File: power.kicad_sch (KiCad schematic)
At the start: 83 parts, among them Q1 BSS138AKA, Q2 SQS401EN-T1_BE3, Q3 BCM857BS-7-F, U3 LMR62014XMF, U4 AP62301_TSOT, U5 AP62301_TSOT, U6 AP22615A_TSOT26

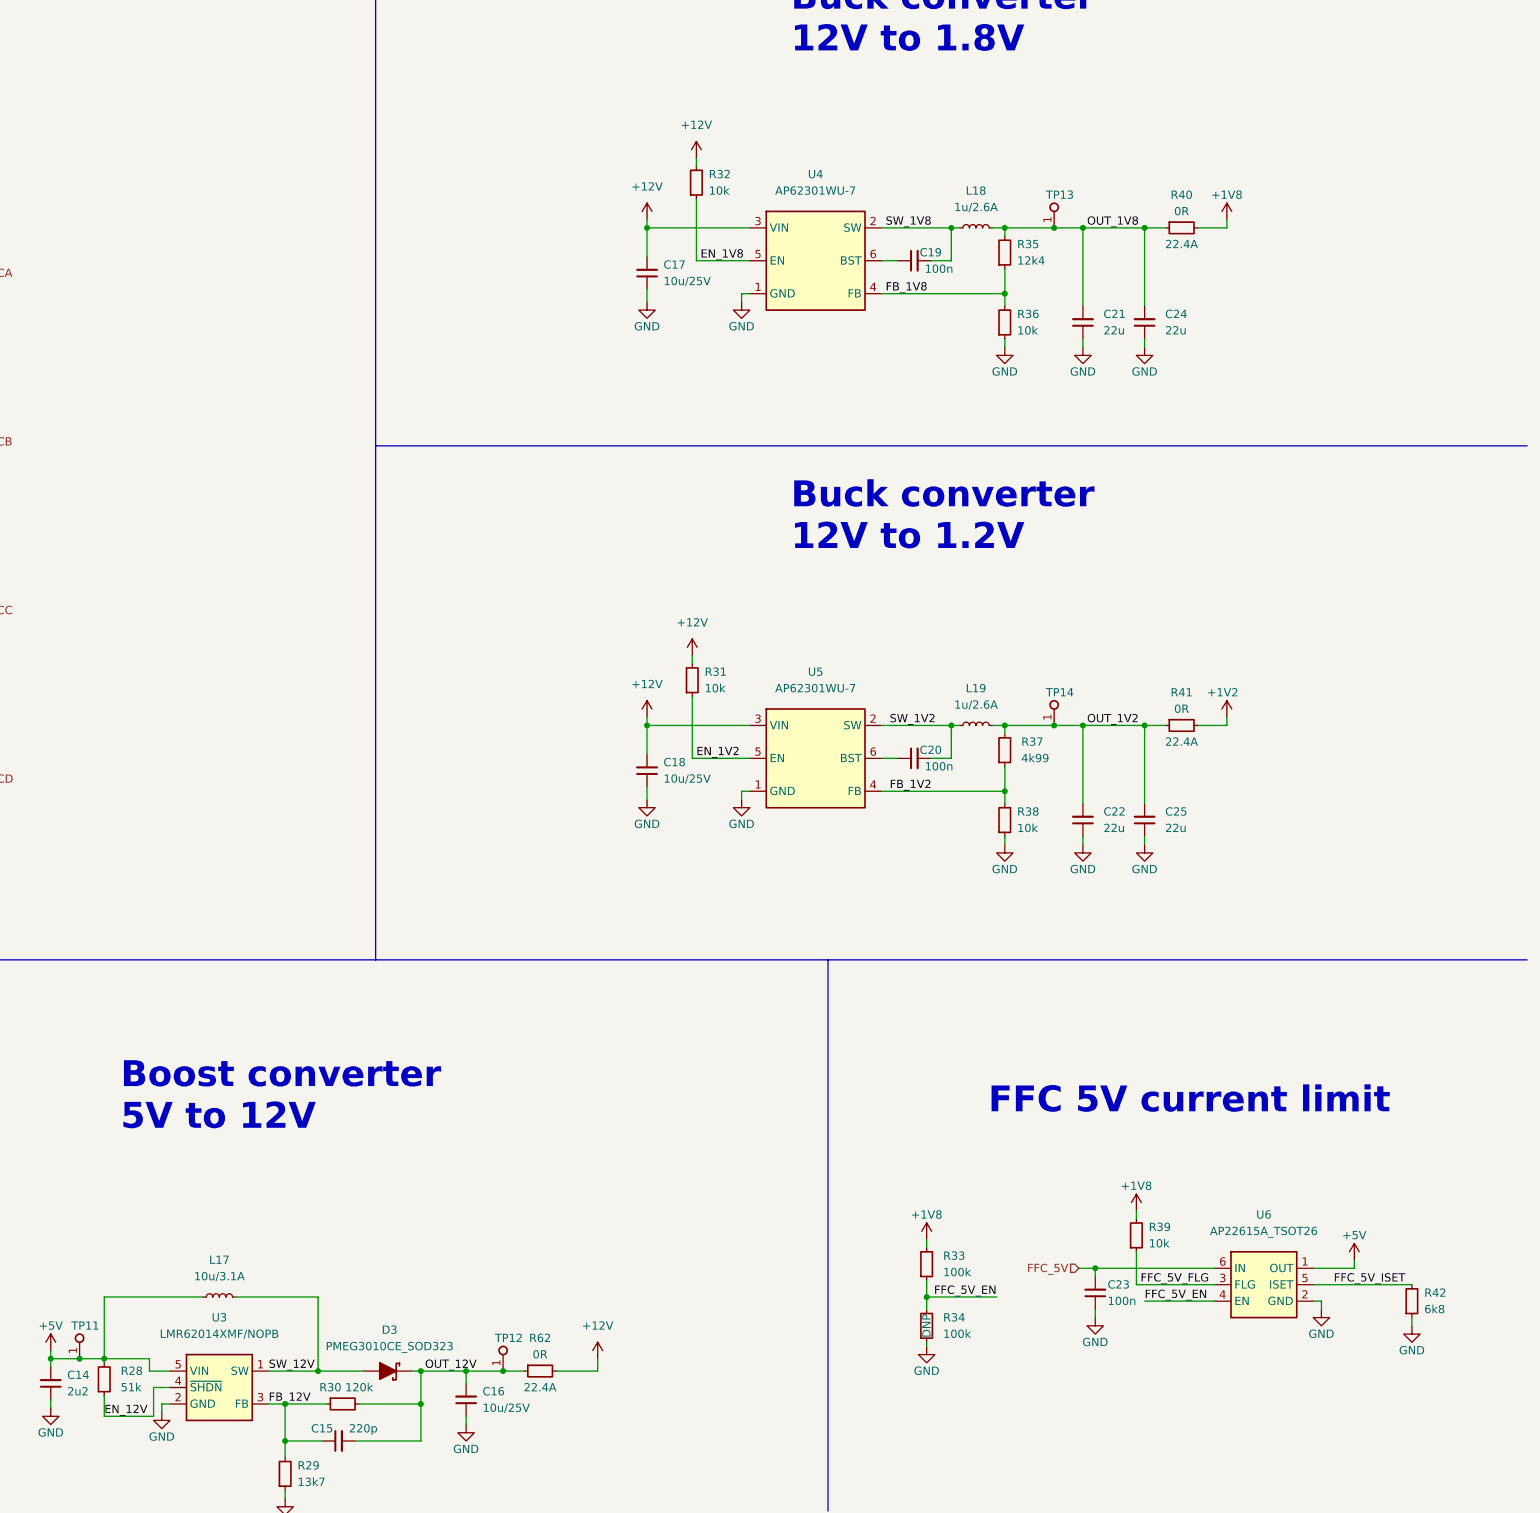
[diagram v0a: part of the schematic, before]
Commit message: Update date, Power: replace 5V_EN and 12V_EN resistors, add capacitors close to current limit switch
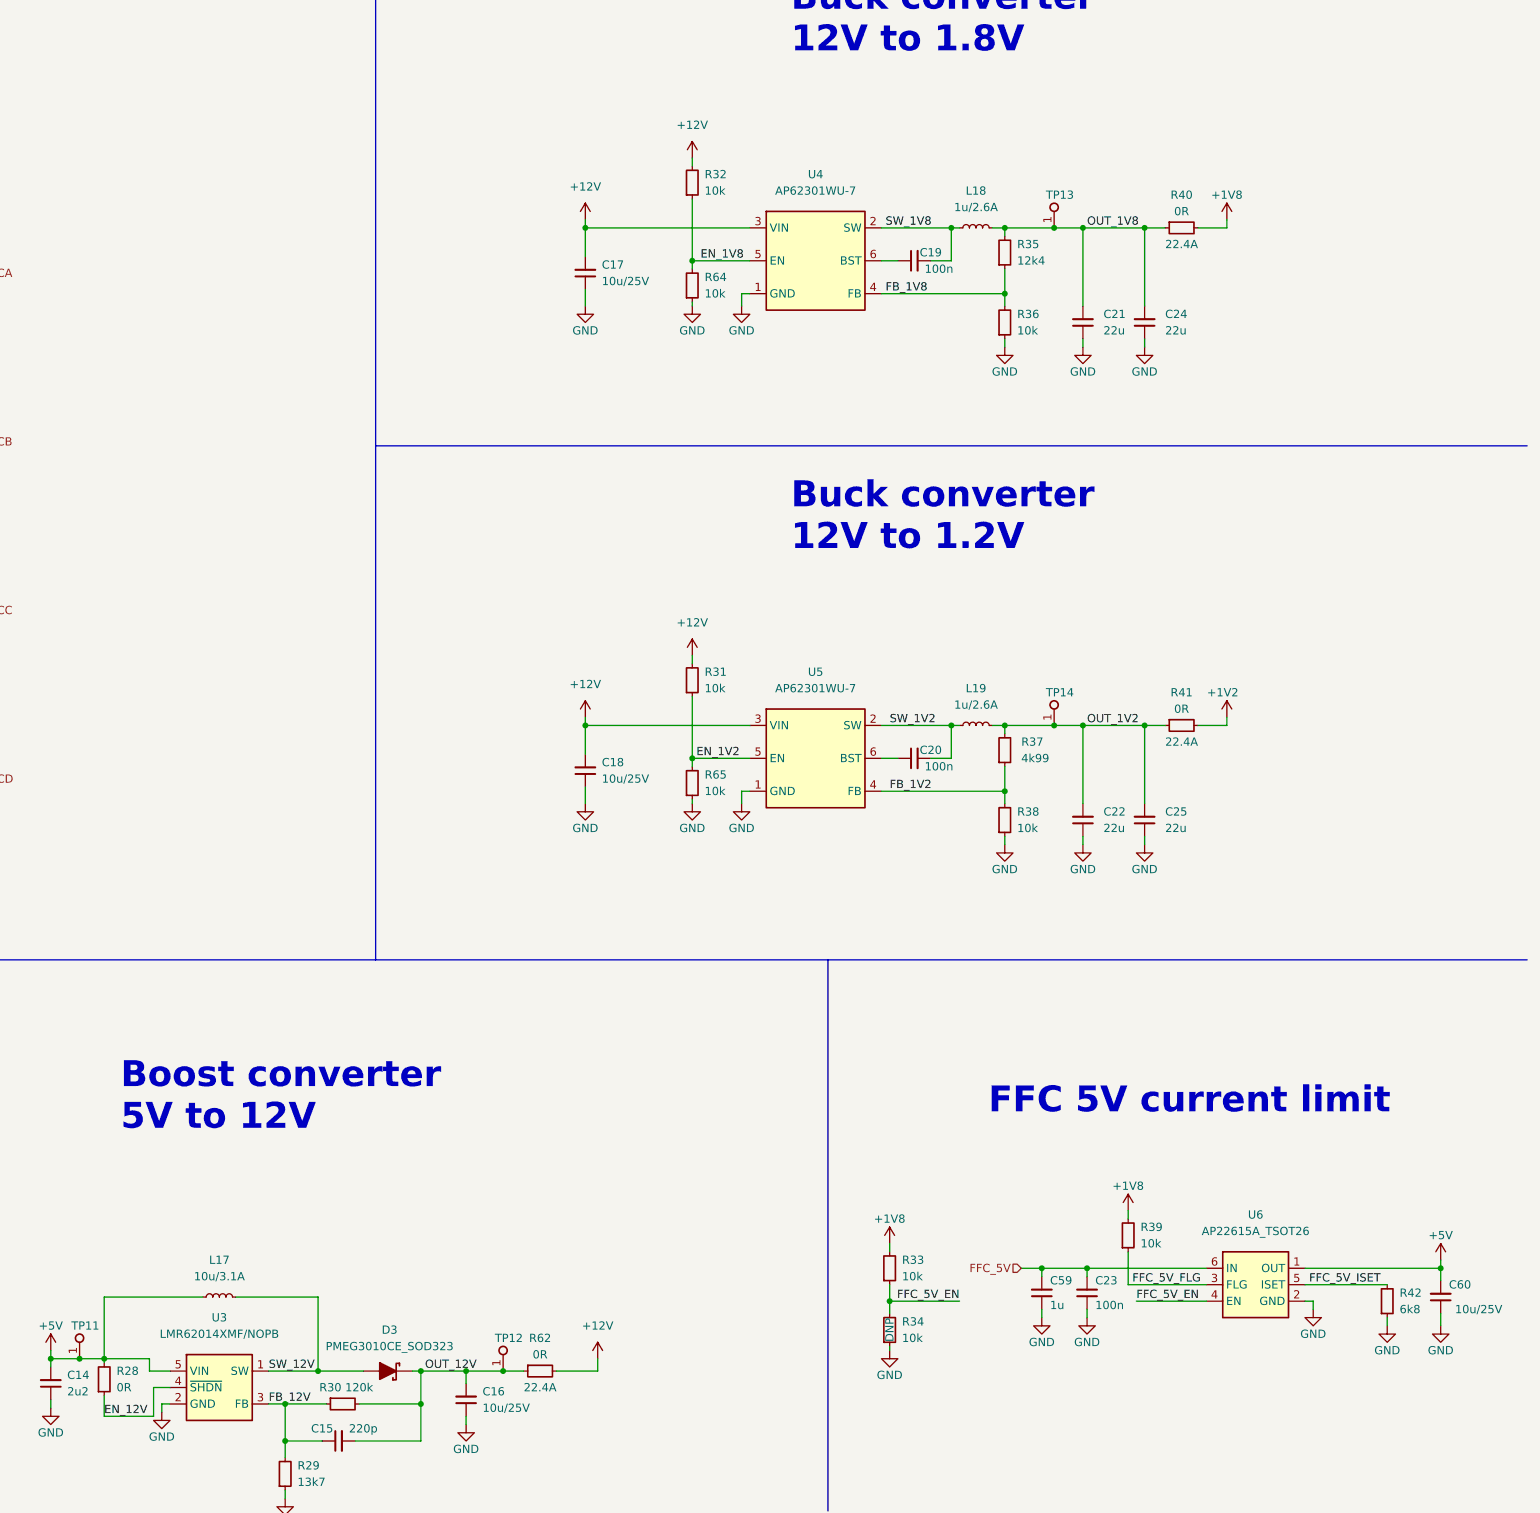
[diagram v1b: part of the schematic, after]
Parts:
- removed R28: R_51k_0402, antmicro-footprints:R_0402_1005Metric, symbol antmicroResistors0402:R_51k_0402
- removed R33, R34: R_100k_0402, antmicro-footprints:R_0402_1005Metric, symbol antmicroResistors0402:R_100k_0402
- added C59: C_1u_0402, antmicro-footprints:C_0402_1005Metric, symbol antmicroCapacitors0402:C_1u_0402
- added C60: C_10u_25V_0603, antmicro-footprints:C_0603_1608Metric, symbol antmicroCapacitors0603:C_10u_25V_0603
- added R28: R_0R_0402, antmicro-footprints:R_0402_1005Metric, symbol antmicroResistors0402:R_0R_0402
- added R33, R34, R64, R65: R_10k_0402, antmicro-footprints:R_0402_1005Metric, symbol antmicroResistors0402:R_10k_0402
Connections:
- net +1V8: now also R33.2
- net +5V: now also C60.2, R28.2
- net EN_12V: now also R28.1
- net EN_1V2: now also R65.2
- net EN_1V8: now also R64.2
- net FFC_5V: now also C59.2
- net FFC_5V_EN: now also R33.1, R34.2
- net GND: now also C59.1, C60.1, R34.1, R64.1, R65.1
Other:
- moved on the sheet: C17, C18, C23, R32, R39, R42, U6

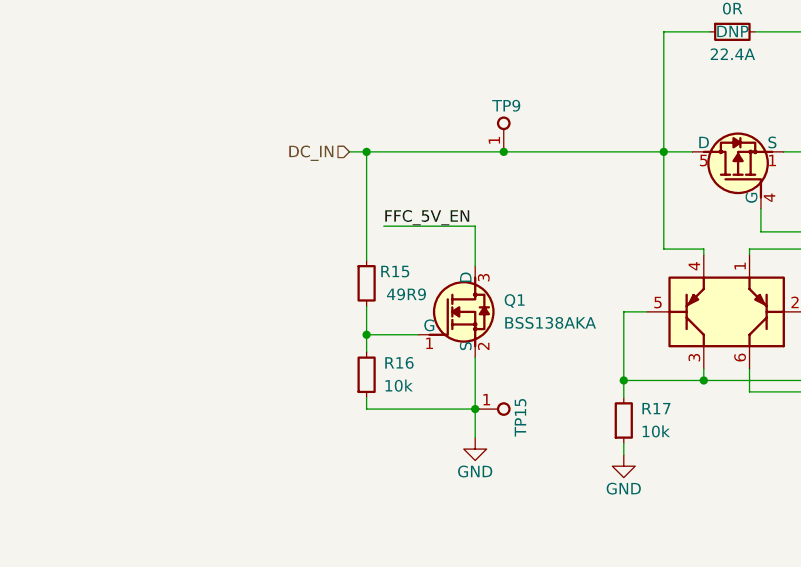
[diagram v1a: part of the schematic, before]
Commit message: Power: replace 49.9R resistor in power arbiter with 100R
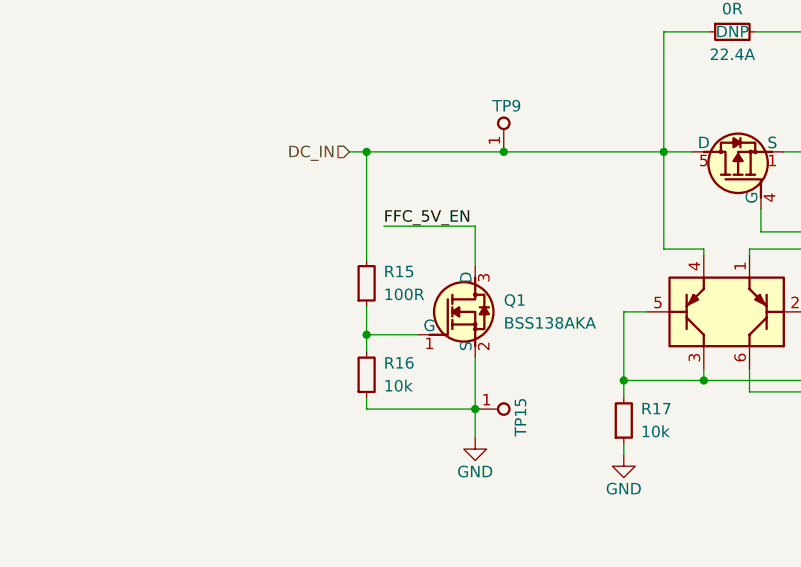
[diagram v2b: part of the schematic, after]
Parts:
- removed R15: R_49R9_0402, antmicro-footprints:R_0402_1005Metric, symbol antmicroResistors0402:R_49R9_0402
- added R15: R_100R_0402, antmicro-footprints:R_0402_1005Metric, symbol antmicroResistors0402:R_100R_0402
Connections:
- net DC_IN: now also R15.2
- net at Q1.1 (G), R16.2: now also R15.1
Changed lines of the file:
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@@
+    (pin "2")
+  )
+  (symbol (lib_id "antmicroResistors0402:R_100R_0402") (at 50.8 241.935 90) (unit 1)
+    (in_bom yes) (on_board yes) (fields_autoplaced)
+    (property "Reference" "R15" (id 0) (at 52.705 238.1249 90)
+      (effects (font (size 1.27 1.27) (thickness 0.15)) (justify right))
+    )
+    (property "Value" "R_100R_0402" (id 1) (at 63.5 221.615 0)
+      (effects (font (size 1.27 1.27) (thickness 0.15)) (justify left bottom) hide)
+    )
+    (property "Footprint" "antmicro-footprints:R_0402_1005Metric" (id 2) (at 66.04 221.615 0)
+      (effects (font (size 1.27 1.27) (thickness 0.15)) (justify left bottom) hide)
+    )
+    (property "Datasheet" "https://www.bourns.com/docs/product-datasheets/cr.pdf" (id 3) (at 68.58 221.615 0)
+      (effects (font (size 1.27 1.27) (thickness 0.15)) (justify left bottom) hide)
+    )
+    (property "MPN" "CR0402-FX-1000GLF" (id 4) (at 71.12 221.615 0)
+      (effects (font (size 1.27 1.27) (thickness 0.15)) (justify left bottom) hide)
+    )
+    (property "Manufacturer" "Bourns" (id 5) (at 73.66 221.615 0)
+      (effects (font (size 1.27 1.27) (thickness 0.15)) (justify left bottom) hide)
+    )
+    (property "License" "Apache-2.0" (id 6) (at 76.2 221.615 0)
+      (effects (font (size 1.27 1.27) (thickness 0.15)) (justify left bottom) hide)
+    )
+    (property "Author" "Antmicro" (id 7) (at 78.74 221.615 0)
+      (effects (font (size 1.27 1.27) (thickness 0.15)) (justify left bottom) hide)
+    )
+    (property "Val" "100R" (id 8) (at 52.705 240.6649 90)
+      (effects (font (size 1.27 1.27) (thickness 0.15)) (justify right))
+    )
+    (property "Tolerance" "1%" (id 9) (at 60.96 221.615 0)
+      (effects (font (size 1.27 1.27)) (justify left bottom) hide)
+    )
+    (pin "1")
     (pin "2")
   )
@@
     (pin "1")
   )
-  (symbol (lib_id "antmicroResistors0402:R_49R9_0402") (at 50.8 236.855 90) (mirror x) (unit 1)
-    (in_bom yes) (on_board yes)
-    (property "Reference" "R15" (id 0) (at 53.975 238.125 90)
-      (effects (font (size 1.27 1.27) (thickness 0.15)))
-    )
-    (property "Value" "R_49R9_0402" (id 1) (at 63.5 257.175 0)
-      (effects (font (size 1.27 1.27) (thickness 0.15)) (justify left bottom) hide)
-    )
-    (property "Footprint" "antmicro-footprints:R_0402_1005Metric" (id 2) (at 66.04 257.175 0)
-      (effects (font (size 1.27 1.27) (thickness 0.15)) (justify left bottom) hide)
-    )
-    (property "Datasheet" "https://www.bourns.com/docs/product-datasheets/cr.pdf" (id 3) (at 68.58 257.175 0)
-      (effects (font (size 1.27 1.27) (thickness 0.15)) (justify left bottom) hide)
-    )
-    (property "MPN" "CR0402-FX-49R9GLF" (id 4) (at 71.12 257.175 0)
-      (effects (font (size 1.27 1.27) (thickness 0.15)) (justify left bottom) hide)
-    )
-    (property "Manufacturer" "Bourns" (id 5) (at 73.66 257.175 0)
-      (effects (font (size 1.27 1.27) (thickness 0.15)) (justify left bottom) hide)
-    )
-    (property "License" "Apache-2.0" (id 6) (at 76.2 257.175 0)
-      (effects (font (size 1.27 1.27) (thickness 0.15)) (justify left bottom) hide)
-    )
-    (property "Author" "Antmicro" (id 7) (at 78.74 257.175 0)
-      (effects (font (size 1.27 1.27) (thickness 0.15)) (justify left bottom) hide)
-    )
-    (property "Val" "49R9" (id 8) (at 55.245 240.665 90)
-      (effects (font (size 1.27 1.27) (thickness 0.15)))
-    )
-    (property "Tolerance" "1%" (id 9) (at 60.96 257.175 0)
-      (effects (font (size 1.27 1.27)) (justify left bottom) hide)
-    )
-    (pin "1")
-    (pin "2")
-  )
   (symbol (lib_id "antmicroResistors0402:R_10k_0402") (at 279.4 143.51 90) (unit 1)
